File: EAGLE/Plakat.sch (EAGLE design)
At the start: 25 parts, among them X1 USB-MICROB

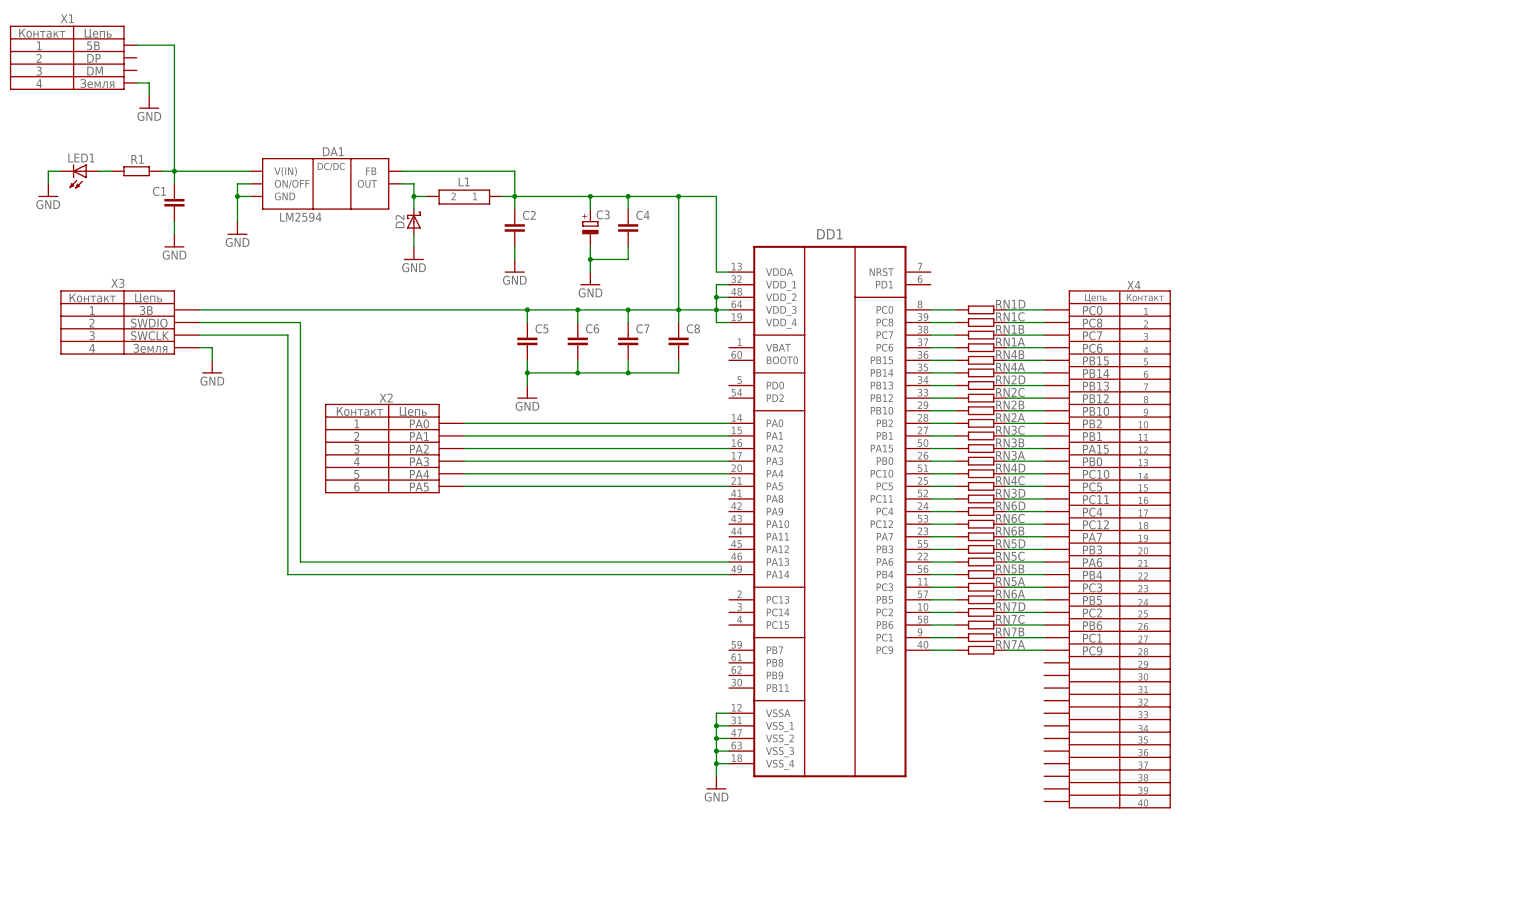
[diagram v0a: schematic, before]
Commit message: Plakat.sch was redrawed by the right way
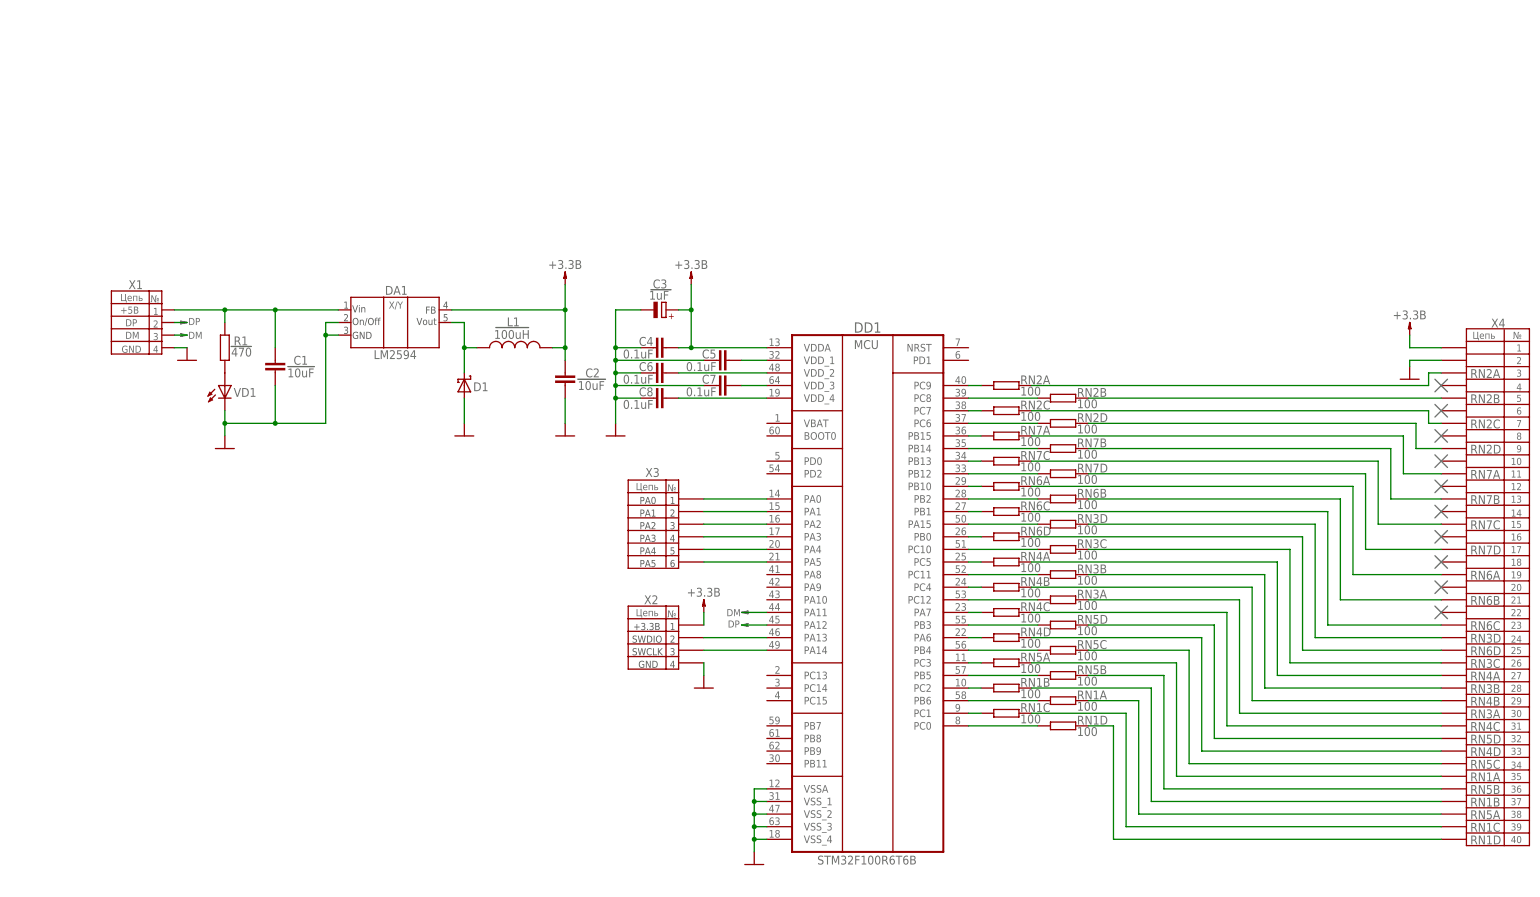
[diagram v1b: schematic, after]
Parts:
- removed D2: 1N5819-T, diode:1N5819-T
- removed LED1: (no value), eagle-ltspice:LED_E
- added D1: 1N5819-T, diode:1N5819-T
- added VD1: (no value), eagle-ltspice:LED_E
- C4, C5, C6, C7, C8: value 100nF -> 0.1uF
- X2: device pinhead:PINHD-1X6 -> pinhead:PINHD-1X4
- X3: device pinhead:PINHD-1X4 -> pinhead:PINHD-1X6
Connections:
- removed net N$33 (its old number): DD1.PB4, RN5B.2
- removed net N$38 (its old number): DD1.PC1, RN7B.2
- removed net N$67: RN7A.1, X4.28
- new net DM: DD1.PA11, X1.D-
- new net DP: DD1.PA12, X1.D+
- new net N$30: C5.2, DD1.VDD_1
- new net N$31: DD1.PA6, RN4D.2
- new net N$34: DD1.PB5, RN5B.2
- new net N$5: DD1.PC9, RN2A.1
- new net N$68: C7.2, DD1.VDD_3
- new net N$69: C6.2, DD1.VDD_2
- new net VCC: C2.1, C3.+, C4.2, DA1.FB, DD1.VDDA, L1.1, X2.1, X4.1
- net GND: now also C4.1, C5.1, C6.1, C7.1, C8.1, D1.A, VD1.C, X2.4, X4.2; no longer C4.2, C5.2, C6.2, C7.2, C8.2, D2.A, DD1.VSSA, DD1.VSS_1, DD1.VSS_2, DD1.VSS_3, DD1.VSS_4, LED1.C, X3.4
- net N$1: now also X1.VBUS; no longer X1.D+
- net N$10: now also X3.5; no longer X2.5
- net N$11: now also X3.6; no longer X2.6
- net N$12: now also RN2C.1; no longer RN1B.1
- net N$13: now also RN2D.1; no longer RN1A.1
- net N$14: now also RN7A.2; no longer RN4B.1
- net N$15: now also RN7B.2; no longer RN4A.1
- net N$16: now also RN7C.2; no longer RN2D.1
- net N$17: now also RN7D.2; no longer RN2C.1
- net N$18: now also RN6A.2; no longer RN2B.1
- net N$19: now also RN6B.2; no longer RN2A.1
- net N$2: now also D1.C; no longer D2.C
- net N$20: now also RN6C.2; no longer RN3C.1
- net N$21: now also RN3D.2; no longer RN3B.1
- net N$22: now also RN6D.2; no longer RN3A.1
- net N$23: now also RN3C.1; no longer RN4D.2
- net N$24: now also RN4A.1; no longer RN4C.2
- net N$25: now also RN3B.1; no longer RN3D.2
- net N$26: now also RN4B.1; no longer RN6D.2
- net N$27: now also RN3A.1; no longer RN6C.2
- net N$28: now also RN4C.2; no longer RN6B.2
- net N$3: now also X3.1; no longer X2.1
- net N$32: now also DD1.PB4; no longer DD1.PA6
- net N$35: now also DD1.PC2, RN1B.1; no longer DD1.PB5, RN6A.2
- net N$36: now also DD1.PB6, RN1A.1; no longer DD1.PC2, RN7D.2
- net N$37: now also DD1.PC1, RN1C.1; no longer DD1.PB6, RN7C.2
- net N$39: now also RN2A.2, X4.3; no longer DD1.PC9, RN7A.2
- net N$4: now also VD1.A; no longer LED1.A
- net N$40: now also RN2B.2, X4.5; no longer RN1D.2, X4.1
- net N$41: now also RN2C.2, X4.7; no longer RN1C.2, X4.2
- net N$42: now also RN2D.2, X4.9; no longer RN1B.2, X4.3
- net N$43: now also RN7A.1, X4.11; no longer RN1A.2, X4.4
- net N$44: now also RN7B.1, X4.13; no longer RN4B.2, X4.5
- net N$45: now also RN7C.1, X4.15; no longer RN4A.2, X4.6
- net N$46: now also RN7D.1, X4.17; no longer RN2D.2, X4.7
- net N$47: now also RN6A.1, X4.19; no longer RN2C.2, X4.8
- net N$48: now also RN6B.1, X4.21; no longer RN2B.2, X4.9
- net N$49: now also RN6C.1, X4.23; no longer RN2A.2, X4.10
- net N$50: now also RN3D.1, X4.24; no longer RN3C.2, X4.11
- net N$51: now also RN6D.1, X4.25; no longer RN3B.2, X4.12
- net N$52: now also RN3C.2, X4.26; no longer RN3A.2, X4.13
- net N$53: now also RN4A.2, X4.27; no longer RN4D.1, X4.14
- net N$54: now also RN3B.2, X4.28; no longer RN4C.1, X4.15
- net N$55: now also RN4B.2, X4.29; no longer RN3D.1, X4.16
- net N$56: now also RN3A.2, X4.30; no longer RN6D.1, X4.17
- net N$57: now also RN4C.1, X4.31; no longer RN6C.1, X4.18
- net N$58: now also RN5D.1, X4.32; no longer RN6B.1, X4.19
- net N$59: now also RN4D.1, X4.33; no longer RN5D.1, X4.20
- net N$6: now also X3.2; no longer X2.2
- net N$60: now also X4.34; no longer X4.21
- net N$61: now also RN5A.1, X4.35; no longer RN5B.1, X4.22
- net N$62: now also RN5B.1, X4.36; no longer RN5A.1, X4.23
- net N$63: now also RN1B.2, X4.37; no longer RN6A.1, X4.24
- net N$64: now also RN1A.2, X4.38; no longer RN7D.1, X4.25
- net N$65: now also RN1C.2, X4.39; no longer RN7C.1, X4.26
- net N$66: now also RN1D.2, X4.40; no longer RN7B.1, X4.27
- net N$7: now also RN2B.1; no longer RN1C.1
- net N$71: now also C8.2; no longer C2.1, C3.+, C4.1, C5.1, C6.1, C7.1, C8.1, DA1.FB, DD1.VDDA, DD1.VDD_1, DD1.VDD_2, DD1.VDD_3, L1.1, X3.1
- net N$8: now also X3.3; no longer X2.3
- net N$9: now also X3.4; no longer X2.4
- net SWCLK: now also X2.3; no longer X3.3
- net SWDIO: now also X2.2; no longer X3.2
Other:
- note added: "+3.3В"
- note added: "+5В"
- note added: "FB"
- note added: "GND"
- note added: "MCU"
- note added: "On/Off"
- note added: "RN1A"
- note added: "RN1B"
- note added: "RN1C"
- note added: "RN1D"
- note added: "RN2A"
- note added: "RN2B"
- note added: "RN2C"
- note added: "RN2D"
- note added: "RN3A"
- note added: "RN3B"
- note added: "RN3C"
- note added: "RN3D"
- note added: "RN4A"
- note added: "RN4B"
- note added: "RN4C"
- note added: "RN4D"
- note added: "RN5A"
- note added: "RN5B"
- note added: "RN5C"
- note added: "RN5D"
- note added: "RN6A"
- note added: "RN6B"
- note added: "RN6C"
- note added: "RN6D"
- note added: "RN7A"
- note added: "RN7B"
- note added: "RN7C"
- note added: "RN7D"
- note added: "STM32F100R6T6B"
- note added: "Vin"
- note added: "Vout"
- note added: "№"
- note removed: "3В"
- note removed: "5В"
- note removed: "PA15"
- note removed: "PA6"
- note removed: "PA7"
- note removed: "PB0"
- note removed: "PB1"
- note removed: "PB10"
- note removed: "PB12"
- note removed: "PB13"
- note removed: "PB14"
- note removed: "PB15"
- note removed: "PB2"
- note removed: "PB3"
- note removed: "PB4"
- note removed: "PB5"
- note removed: "PB6"
- note removed: "PC0"
- note removed: "PC1"
- note removed: "PC10"
- note removed: "PC11"
- note removed: "PC12"
- note removed: "PC2"
- note removed: "PC3"
- note removed: "PC4"
- note removed: "PC5"
- note removed: "PC6"
- note removed: "PC7"
- note removed: "PC8"
- note removed: "PC9"
- note removed: "Земля"
- note removed: "Контакт"
- moved on the sheet: C1, C2, C3, C4, C5, C6, C7, C8, DD1, R1, RN1A, RN1B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

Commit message: Modified СБ, Э3, ПП
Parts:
- removed X1: USB-MICROB, SparkFun-Connectors:USB-MICROB
- added X1.1, X1.2: (no value), pinhead:PINHD-1X2
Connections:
- removed net DM: DD1.PA11, X1.D-
- removed net DP: DD1.PA12, X1.D+
- new net N$67: DD1.PA11
- new net N$70: DD1.PA12
- net GND: now also X1.1.2; no longer X1.GND
- net N$1: now also X1.1.1; no longer X1.VBUS
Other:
- moved on the sheet: C1, C2, C3, C4, C5, C6, C7, C8, D1, DA1, DD1, L1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
